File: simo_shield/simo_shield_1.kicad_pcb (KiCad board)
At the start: 2 copper layers, 64.6 x 82.5 mm, 6 parts, among them J1 CONECTOR DEBUG_UART, J2 VBAT, U1 YAAJ_BluePill_Part_Like_SWD_B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, U2 elemon_board, U3 flash_externa, U4 mpu6050

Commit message: casi terminado, revisar PCB, error de conexion pero no entiendo por que.
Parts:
- U1: footprint simo:YAAJ_BluePill_SWD_1 -> bluepill:YAAJ_BluePill_SWD_1
- moved U1 0.39 mm to (65.0, 70.0)
- renumbered J2 to CONECTOR_BATERIA1
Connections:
- CONECTOR_BATERIA1 pad 1: BAT_EXT -> +BATT
- CONECTOR_BATERIA1 pad 2: GND_BAT -> /BAT_GND
- J1 pad 1: DEBUG_TX -> Net-(J1-Pad1)
- J1 pad 2: DEBUG_RX -> Net-(J1-Pad2)
- U1 pad 1: Net-(U1-Pad1) -> /BAT_ENA_PIN
- U1 pad 19: Net-(U1-Pad19) -> /BAT_GND
- U1 pad 20: Net-(U1-Pad20) -> unconnected-(U1-Pad20)
- U1 pad 21: unconnected-(U1-Pad21) -> +BATT
- U1 pad 27: DEBUG_TX -> Net-(J1-Pad2)
- U1 pad 28: DEBUG_RX -> Net-(J1-Pad1)
- U1 pad 38: Net-(U1-Pad38) -> unconnected-(U1-Pad38)
- U1 pad 39: Net-(U1-Pad39) -> /BAT_GND
- U1 pad 40: Net-(U1-Pad39) -> /BAT_GND
- U1 pad 41: Net-(U1-Pad41) -> unconnected-(U1-Pad41)
- U1 pad 42: Net-(U1-Pad42) -> unconnected-(U1-Pad42)
- U1 pad 43: Net-(U1-Pad43) -> unconnected-(U1-Pad43)
- U1 pad 44: Net-(U1-Pad44) -> unconnected-(U1-Pad44)
- U2 pad 10: GND_BAT -> /BAT_GND
- U2 pad 2: AT_RX -> Net-(U1-Pad7)
- U2 pad 24: GND_BAT -> /BAT_GND
- U2 pad 26: BAT_EXT -> +BATT
- U2 pad 4: AT_TX -> Net-(U1-Pad6)
- U2 pad 52: BAT_ENA -> /BAT_ENA_PIN
- U2 pad 9: PWRUP -> Net-(U1-Pad2)
- U3 pad 1: BAT_EXT -> +BATT
- U3 pad 2: GND_BAT -> /BAT_GND
- U4 pad 5: SCL_MPU6050 -> Net-(U1-Pad36)
- U4 pad 6: SDA_MPU6050 -> Net-(U1-Pad35)
- U4 pad 7: GND_BAT -> /BAT_GND
- U4 pad 8: BAT_EXT -> +BATT
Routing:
- net /BAT_GND: track 0.00 -> 224.1 mm
- net GND_BAT: track 197.5 -> 0.00 mm
- net +BATT: track 0.00 -> 144.9 mm
- net BAT_EXT: track 137.6 -> 0.00 mm
- net /BAT_ENA_PIN: track 0.00 -> 106.5 mm
- net AT_TX: track 68.1 -> 0.00 mm
- net AT_RX: track 40.1 -> 0.00 mm
- net Net-(U1-Pad2): track 0.00 -> 39.9 mm
- net Net-(U1-Pad16): track 0.00 -> 35.6 mm
- net PWRUP: track 29.8 -> 0.00 mm
- net Net-(U1-Pad6): track 0.00 -> 22.5 mm
- net Net-(J1-Pad1): track 0.00 -> 22.2 mm
- net DEBUG_RX: track 19.3 -> 0.00 mm
- net Net-(U1-Pad36): track 0.00 -> 19.0 mm
- net Net-(J1-Pad2): track 0.00 -> 18.7 mm
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- added copper zone on F.Cu, net /BAT_GND
- removed copper zone on F.Cu, net GND_BAT

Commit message: update en pcb shield
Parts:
- moved U1 2.06 mm to (66.8, 71.0)
- moved CONECTOR_BATERIA 1.80 mm to (93.0, 70.2)
- moved J1 1.80 mm to (91.8, 115.0)
- moved U2 1.80 mm to (49.8, 68.0)
- moved U3 1.80 mm to (62.2, 127.5)
- moved U4 1.80 mm to (88.5, 101.8)
- renumbered CONECTOR_BATERIA1 to CONECTOR_BATERIA
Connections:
- U1 pad 10: unconnected-(U1-Pad10) -> Net-(U2-Pad14)
- U2 pad 14: unconnected-(U2-Pad14) -> Net-(U2-Pad14)
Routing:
- net /BAT_GND: track 224.1 -> 17.9 mm
- net Net-(U1-Pad7): track 17.8 -> 56.9 mm
- net Net-(U1-Pad6): track 22.5 -> 49.4 mm
- net Net-(U2-Pad14): track 0.00 -> 25.2 mm
- net Net-(J1-Pad1): track 22.2 -> 38.5 mm
- net /BAT_ENA_PIN: track 106.5 -> 118.6 mm
- net Net-(U1-Pad2): track 39.9 -> 32.6 mm
- net Net-(U1-Pad12): track 51.1 -> 56.6 mm
- net Net-(U1-Pad13): track 50.0 -> 45.7 mm
- net Net-(U1-Pad36): track 19.0 -> 22.2 mm
- net unconnected-(U2-Pad14): track 3.20 -> 0.00 mm
- net Net-(U1-Pad16): track 35.6 -> 38.8 mm
- net +BATT: track 144.9 -> 143.0 mm
- net Net-(J1-Pad2): track 18.7 -> 19.5 mm
- net Net-(U1-Pad11): track 55.6 -> 56.3 mm
- added copper zone on B.Cu, net /BAT_GND
- removed copper zone on F.Cu, net /BAT_GND

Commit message: simo shield pcb listo para revision
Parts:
- renumbered CONECTOR_BATERIA to CONECTOR_BATERIA1
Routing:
- net Net-(U1-Pad6): track 49.4 -> 51.8 mm
- net Net-(U1-Pad12): track 56.6 -> 55.3 mm
- net +BATT: track 143.0 -> 142.0 mm
- net Net-(U1-Pad2): track 32.6 -> 33.5 mm
- net /BAT_ENA_PIN: track 118.6 -> 119.2 mm
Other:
- board text added: "Drifter Modular SIMO v1"

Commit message: update
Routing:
- net /BAT_ENA_PIN: track 119.2 -> 162.3 mm
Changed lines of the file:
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@@
   (segment (start 106 135.06) (end 109.8 135.06) (width 0.8) (layer "B.Cu") (net 83))
   (segment (start 68.20048 67.79952) (end 111 67.79952) (width 0.4) (layer "B.Cu") (net 83))
-  (segment (start 111.2 67.99952) (end 111.549511 68.349031) (width 0.8) (layer "B.Cu") (net 83))
-  (segment (start 66.8 69.2) (end 68.20048 67.79952) (width 0.4) (layer "B.Cu") (net 83))
-  (segment (start 111.549511 134.450489) (end 110.94 135.06) (width 0.8) (layer "B.Cu") (net 83))
-  (segment (start 111 67.99952) (end 111.2 67.99952) (width 0.8) (layer "B.Cu") (net 83))
-  (segment (start 66.8 71) (end 66.8 69.2) (width 0.4) (layer "B.Cu") (net 83))
-  (segment (start 110.94 135.06) (end 109.8 135.06) (width 0.8) (layer "B.Cu") (net 83))
-  (segment (start 111.549511 68.349031) (end 111.549511 134.450489) (width 0.8) (layer "B.Cu") (net 83))
+  (segment (start 110.94 135.06) (end 111.549511 134.450489) (width 0.8) (layer "B.Cu") (net 83))
+  (segment (start 66.8 71) (end 66.8 69.2) (width 0.8) (layer "B.Cu") (net 83))
+  (segment (start 66.8 69.2) (end 68.00048 67.99952) (width 0.8) (layer "B.Cu") (net 83))
+  (segment (start 111.2 67.99952) (end 68.00048 67.99952) (width 0.8) (layer "B.Cu") (net 83))
+  (segment (start 111.549511 134.450489) (end 111.549511 68.349031) (width 0.8) (layer "B.Cu") (net 83))
+  (segment (start 111.549511 68.349031) (end 111.2 67.99952) (width 0.8) (layer "B.Cu") (net 83))
+  (segment (start 66.5 70.7) (end 66.8 71) (width 0.8) (layer "B.Cu") (net 83))
+  (segment (start 109.8 135.06) (end 110.94 135.06) (width 0.8) (layer "B.Cu") (net 83))
   (segment (start 58 76.5) (end 60.96 73.54) (width 0.8) (layer "B.Cu") (net 84))
   (segment (start 58 94) (end 58 76.5) (width 0.8) (layer "B.Cu") (net 84))

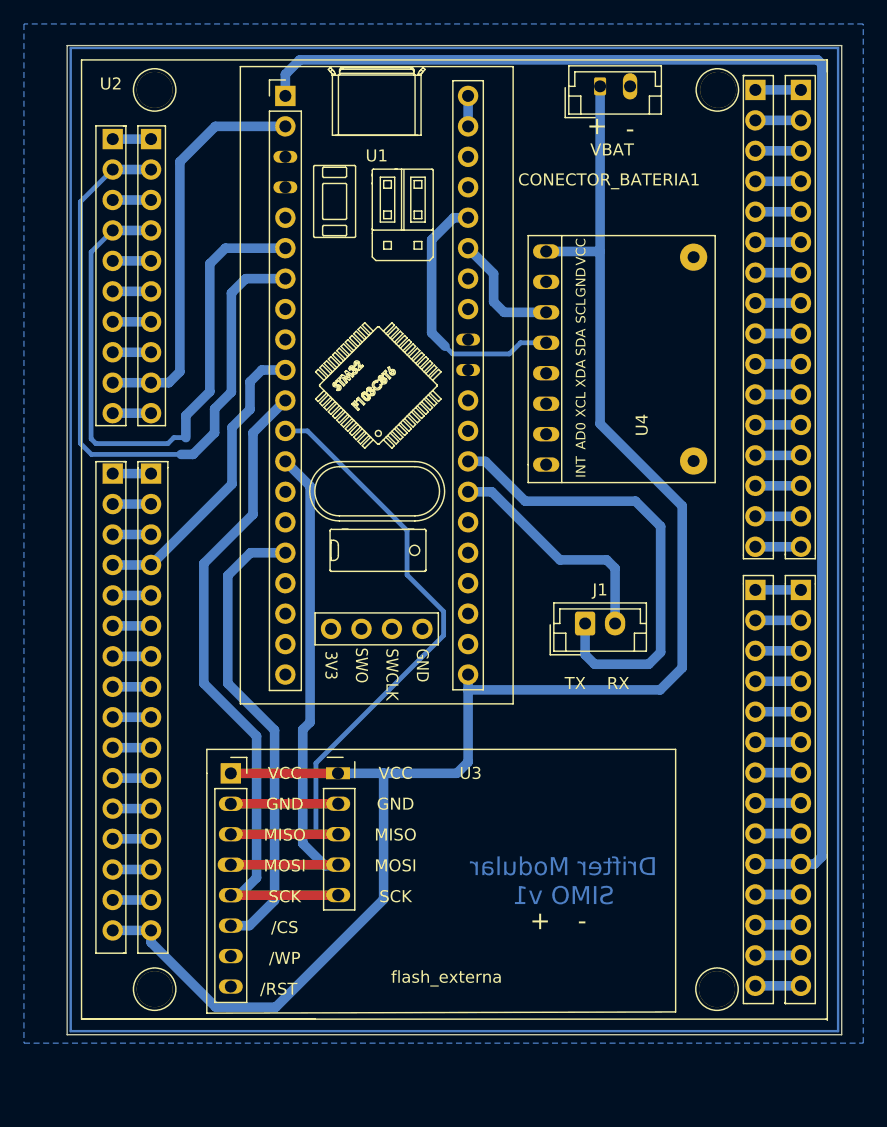
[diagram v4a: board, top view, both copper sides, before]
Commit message: se agrego un circuito para mediciones de tension de bateria mediante la bluepill
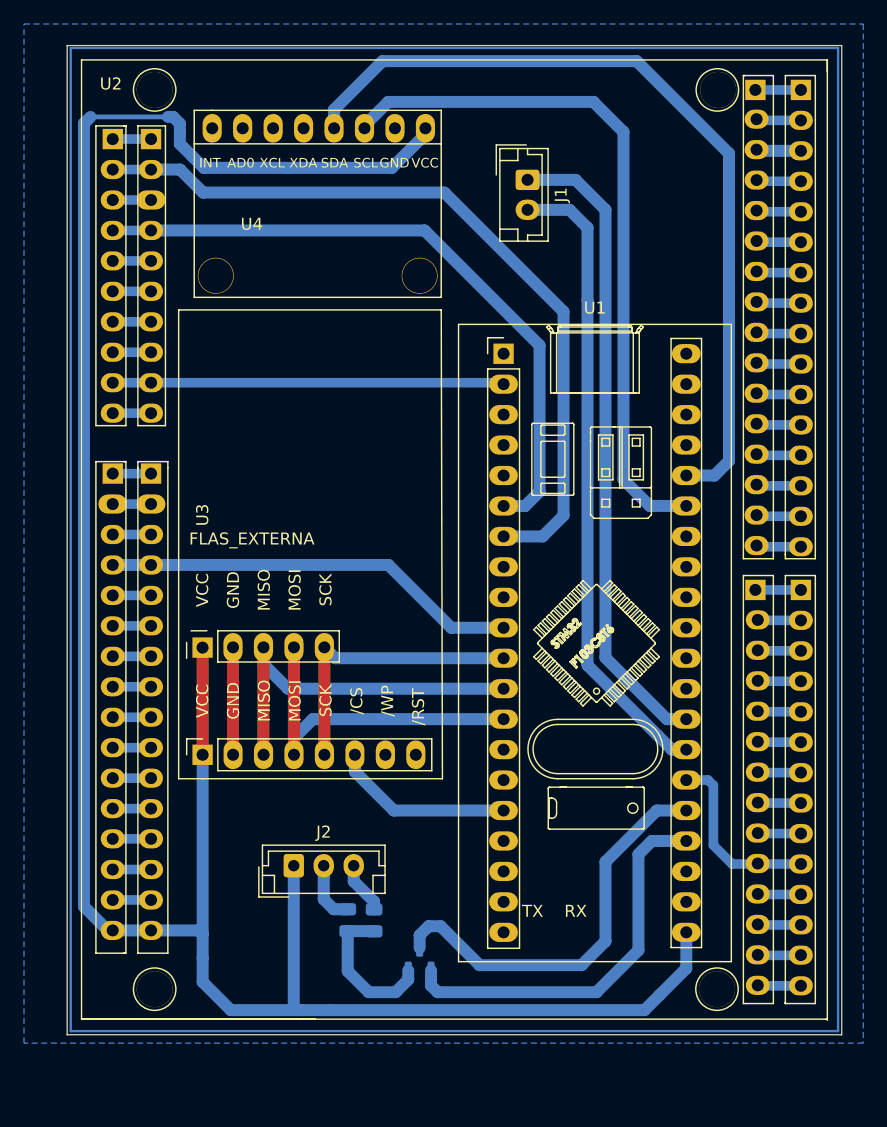
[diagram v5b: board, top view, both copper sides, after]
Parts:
- removed CONECTOR_BATERIA1: VBAT, Connector_JST:JST_EH_B2B-EH-A_1x02_P2.50mm_Vertical
- added J2: CONECTOR BATERIA, Connector_JST:JST_EH_B3B-EH-A_1x03_P2.50mm_Vertical, F.Cu at (67.5, 135.2)
- added Q1: 2N7002E, Package_TO_SOT_SMD:SOT-23, B.Cu at (78.0, 143.0)
- added R1: 150K, Resistor_SMD:R_0805_2012Metric, B.Cu at (74.2, 139.8)
- added R2: 120K, Resistor_SMD:R_0805_2012Metric, B.Cu at (72.0, 139.8)
- U1: footprint bluepill:YAAJ_BluePill_SWD_1 -> bluepill:YAAJ_BluePill_SWD_1_modificado
- U2: value elemon_board -> ELEMON_BOARD; footprint elemon_board:elemon_board -> elemon_board:elemon_board_modificado
- U3: value flash_externa -> FLAS_EXTERNA
- U4: value mpu6050 -> MPU6050
- moved U4 39.5 mm to (60.7, 73.7), turned to 0 degrees
- moved J1 37.3 mm to (87.0, 78.0), turned to -90 degrees
- moved U1 28.2 mm to (85.0, 92.5)
- moved U3 2.82 mm to (59.9, 126.0), turned to 90 degrees
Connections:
- net +BATT renamed /BAT_EXT
- U1 pad 1: /BAT_ENA_PIN -> unconnected-(U1-Pad1)
- U1 pad 24: unconnected-(U1-Pad24) -> Net-(U1-Pad24)
- U1 pad 25: unconnected-(U1-Pad25) -> Net-(U1-Pad25)
- U1 pad 26: unconnected-(U1-Pad26) -> /BAT_ENA_PIN
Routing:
- net /BAT_ENA_PIN: track 162.3 -> 15.4 mm
- net /BAT_EXT: track 142.0 -> 195.1 mm
- net Net-(U1-Pad35): track 10.1 -> 58.8 mm
- net Net-(U1-Pad36): track 22.2 -> 69.1 mm
- net Net-(U1-Pad25): track 0.00 -> 34.2 mm
- net Net-(J1-Pad2): track 19.5 -> 53.3 mm
- net Net-(U1-Pad24): track 0.00 -> 32.7 mm
- net Net-(U1-Pad11): track 56.2 -> 24.3 mm
- net Net-(U1-Pad12): track 55.3 -> 31.2 mm
- net Net-(U1-Pad16): track 38.8 -> 15.1 mm
- net Net-(U1-Pad13): track 45.7 -> 28.5 mm
- net Net-(J1-Pad1): track 38.5 -> 53.8 mm
- net Net-(Q1-Pad2): track 0.00 -> 12.5 mm
- net Net-(U1-Pad10): track 25.2 -> 37.0 mm
- net Net-(U1-Pad7): track 56.7 -> 65.2 mm
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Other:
- board text removed: "+"
- board text removed: "-"
- board text removed: "Drifter Modular SIMO v1"

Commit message: update a placas
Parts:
- moved Q1 0.50 mm to (78.0, 143.5), turned to 0 degrees
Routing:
- net Net-(Q1-Pad2): track 12.5 -> 6.90 mm
- net Net-(Q1-Pad3): track 34.2 -> 30.5 mm
- net Net-(U1-Pad35): track 58.8 -> 60.2 mm
- net Net-(Q1-Pad1): track 32.7 -> 33.6 mm
- net /BAT_EXT: track 195.1 -> 194.3 mm
- net /BAT_ENA_PIN: track 15.4 -> 14.8 mm

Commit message: update
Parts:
- added R3: 2k2, Resistor_SMD:R_0805_2012Metric, B.Cu at (71.0, 132.5)
- R1: value 150K -> 100
- R2: value 120K -> 1K
- moved Q1 6.68 mm to (71.6, 141.6), turned to 180 degrees
- moved R1 6.37 mm to (76.5, 145.7), turned to 0 degrees
- moved J2 6.07 mm to (64.2, 140.3), turned to 90 degrees
- moved R2 5.31 mm to (74.9, 135.3)
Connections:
- net Net-(J1-Pad2) renamed /UART_DEBUG_TX
- J1 pad 1: Net-(J1-Pad1) -> /UART_DEBUG_RX
- Q1 pad 2: Net-(Q1-Pad2) -> /LEVEL_BAT
- R1 pad 1: Net-(Q1-Pad2) -> Net-(Q1-Pad1)
- R1 pad 2: /BAT_SIN_REGULAR -> /SWITCH_BAT
- R2 pad 2: Net-(Q1-Pad2) -> /LEVEL_BAT
- U1 pad 24: Net-(Q1-Pad1) -> /SWITCH_BAT
- U1 pad 25: Net-(Q1-Pad3) -> /LEVEL_BAT
- U1 pad 28: Net-(J1-Pad1) -> /UART_DEBU_RX
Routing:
- net Net-(J1-Pad1): track 53.8 -> 0.00 mm
- net /UART_DEBU_RX: track 0.00 -> 53.8 mm
- net Net-(Q1-Pad1): track 33.6 -> 0.00 mm
- net /SWITCH_BAT: track 0.00 -> 32.8 mm
- net Net-(Q1-Pad3): track 30.5 -> 0.00 mm
- net /LEVEL_BAT: track 0.00 -> 27.9 mm
- net /BAT_EXT: track 194.3 -> 182.1 mm
- net /BAT_GND: track 22.3 -> 15.4 mm
- net Net-(Q1-Pad2): track 6.90 -> 0.00 mm
- net /BAT_SIN_REGULAR: track 4.35 -> 0.00 mm

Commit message: update simo_shield
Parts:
- removed Q1: 2N7002E, Package_TO_SOT_SMD:SOT-23
- removed R3: 2k2, Resistor_SMD:R_0805_2012Metric
- added J2: CONECTOR BATERIA, Connector_JST:JST_EH_B2B-EH-A_1x02_P2.50mm_Vertical, F.Cu at (72.5, 140.0)
- R1: value 100 -> 365K; moved to F.Cu
- R2: value 1K -> 155K; moved to F.Cu
- moved R2 10.6 mm to (80.2, 144.5), turned to 90 degrees
- moved R1 1.30 mm to (77.0, 144.5), turned to -90 degrees
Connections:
- R1 pad 2: /SWITCH_BAT -> Net-(U1-Pad25)
- R2 pad 1: /BAT_GND -> Net-(U1-Pad25)
- R2 pad 2: /LEVEL_BAT -> /GND_ELEMON
- U1 pad 19: /BAT_GND -> /GND_ELEMON
- U1 pad 21: /BAT_EXT -> /USB33_ELEMON
- U1 pad 24: /SWITCH_BAT -> unconnected-(U1-Pad24)
- U1 pad 25: /LEVEL_BAT -> Net-(U1-Pad25)
- U1 pad 39: /BAT_GND -> /GND_ELEMON
- U1 pad 40: /BAT_GND -> /GND_ELEMON
- U2 pad 23: unconnected-(U2-Pad23) -> /USB33_ELEMON
- U2 pad 24: /BAT_GND -> /GND_ELEMON
- U2 pad 26: /BAT_EXT -> unconnected-(U2-Pad26)
- U3 pad 1: /BAT_EXT -> /GND_ELEMON
- U3 pad 2: /BAT_GND -> /USB33_ELEMON
- U4 pad 7: /BAT_GND -> /GND_ELEMON
- U4 pad 8: /BAT_EXT -> /USB33_ELEMON
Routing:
- net unconnected-(U2-Pad26): track 0.00 -> 182.1 mm
- net /BAT_EXT: track 182.1 -> 0.00 mm
- net Net-(U1-Pad25): track 0.00 -> 32.9 mm
- net /SWITCH_BAT: track 32.8 -> 0.00 mm
- net /LEVEL_BAT: track 27.9 -> 0.00 mm
- net /GND_ELEMON: track 0.00 -> 21.4 mm
- net /USB33_ELEMON: track 0.00 -> 12.2 mm
- net /BAT_GND: track 15.4 -> 3.20 mm
- net Net-(J2-Pad1): track 0.00 -> 5.99 mm
- net unconnected-(U2-Pad23): track 3.20 -> 0.00 mm
